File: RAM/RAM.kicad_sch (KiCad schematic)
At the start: 44 parts, among them J1 Conn_01x02_Pin, J2 Conn_01x01_Pin, J3 Conn_01x02_Pin, J4 Conn_01x01_Pin, J5 Conn_01x05_Pin, J6 Conn_01x03_Pin, J7 Conn_01x03_Pin, J8 Conn_01x03_Pin, J9 Conn_01x10_Pin, U2 CD74HCT258E, U3 SN74HCT245N, U4 CD74HCT258E, U6 CD74HCT258E

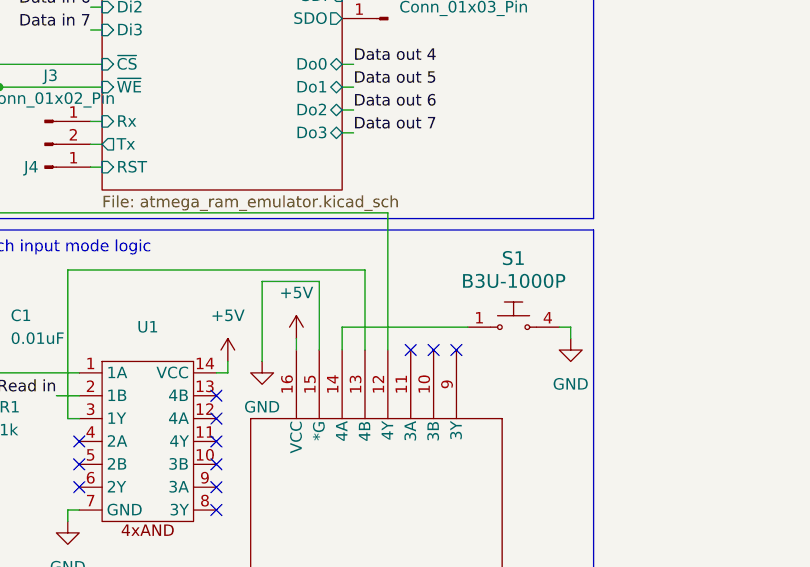
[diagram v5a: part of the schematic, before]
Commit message: Added a pull up resistor to the programming button
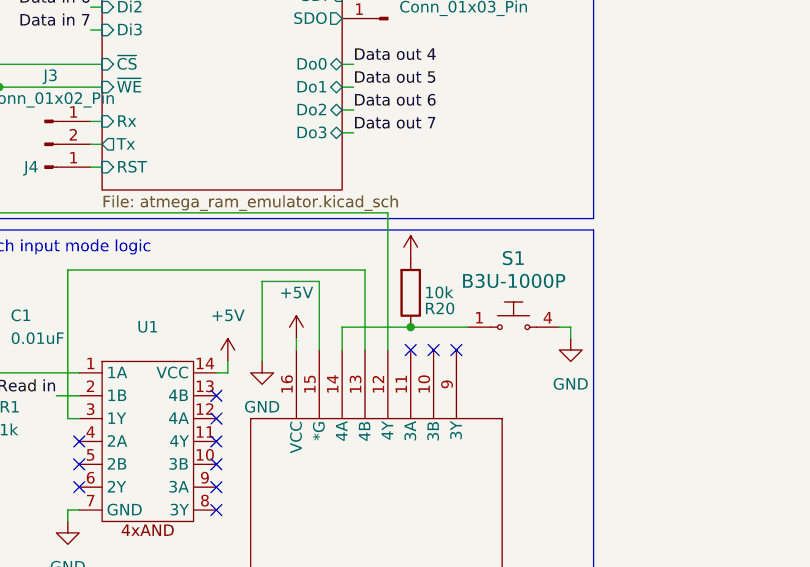
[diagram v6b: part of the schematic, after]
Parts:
- added R20: 10k, _DownloadFootprints:CF_series_Resistors_THT, symbol Device:R
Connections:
- net +5V: now also R20.2
- net at S1.1, U2.14 (4A): now also R20.1
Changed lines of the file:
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@@
 	)
 	(junction
+		(at 71.12 123.19)
+		(diameter 0)
+		(color 0 0 0 0)
+	)
+	(junction
 		(at 210.82 153.67)
 		(diameter 0)
@@
 	(wire
 		(pts
-			(xy 63.5 123.19) (xy 77.47 123.19)
+			(xy 63.5 123.19) (xy 71.12 123.19)
 		)
 		(stroke
@@
 	(wire
 		(pts
+			(xy 71.12 123.19) (xy 77.47 123.19)
+		)
+		(stroke
+			(width 0)
+			(type default)
+		)
+	)
+	(wire
+		(pts
 			(xy 203.2 152.4) (xy 203.2 153.67)
 		)
@@
 	(symbol
 		(lib_id "power:+5V")
+		(at 71.12 115.57 0)
+		(unit 1)
+		(exclude_from_sim no)
+		(in_bom yes)
+		(on_board yes)
+		(dnp no)
+		(fields_autoplaced yes)
+		(property "Reference" "#PWR033"
+			(at 71.12 119.38 0)
+			(effects
+				(font
+					(size 1.27 1.27)
+				)
+				(hide yes)
+			)
+		)
+		(property "Value" "+5V"
+			(at 71.12 110.49 0)
+			(effects
+				(font
+					(size 1.27 1.27)
+				)
+				(hide yes)
+			)
+		)
+		(property "Footprint" ""
+			(at 71.12 115.57 0)
+			(effects
+				(font
+					(size 1.27 1.27)
+				)
+				(hide yes)
+			)
+		)
+		(property "Datasheet" ""
+			(at 71.12 115.57 0)
+			(effects
+				(font
+					(size 1.27 1.27)
+				)
+				(hide yes)
+			)
+		)
+		(property "Description" "Power symbol creates a global label with name \"+5V\""
+			(at 71.12 115.57 0)
+			(effects
+				(font
+					(size 1.27 1.27)
+				)
+				(hide yes)
+			)
+		)
+		(pin "1"
+		)
+		(instances
+			(project ""
+				(path "/5d332551-33f6-4491-a826-882274bc7f5d"
+					(reference "#PWR033")
+					(unit 1)
+				)
+			)
+		)
+	)
+	(symbol
+		(lib_id "power:+5V")
 		(at 50.8 127 0)
 		(unit 1)
@@
 					(unit 1)
 				)
+			)
+		)
+	)
+	(symbol
+		(lib_id "Device:R")
+		(at 71.12 119.38 0)
+		(mirror x)
+		(unit 1)
+		(exclude_from_sim no)
+		(in_bom yes)
+		(on_board yes)
+		(dnp no)
+		(property "Reference" "R20"
+			(at 72.644 121.158 0)
+			(effects
+				(font
+					(size 1.27 1.27)
+				)
+				(justify left)
+			)
+		)
+		(property "Value" "10k"
+			(at 72.644 119.38 0)
+			(effects
+				(font
+					(size 1.27 1.27)
+				)
+				(justify left)
+			)
+		)
+		(property "Footprint" "_DownloadFootprints:CF_series_Resistors_THT"
+			(at 69.342 119.38 90)
+			(effects
+				(font
+					(size 1.27 1.27)
+				)
+				(hide yes)
+			)
+		)
+		(property "Datasheet" "~"
+			(at 71.12 119.38 0)
+			(effects
+				(font
+					(size 1.27 1.27)
+				)
+				(hide yes)
+			)
+		)
+		(property "Description" "Resistor"
+			(at 71.12 119.38 0)
+			(effects
+				(font
+					(size 1.27 1.27)
+				)
+				(hide yes)
+			)
+		)
+		(pin "2"
+		)
+		(pin "1"
+		)
+		(instances
+			(project "RAM"
+				(path "/5d332551-33f6-4491-a826-882274bc7f5d"
+					(reference "R20")
+					(unit 1)
+				)
